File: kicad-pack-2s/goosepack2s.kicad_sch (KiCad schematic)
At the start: 67 parts, among them J1 USB_C_Receptacle_USB2.0_16P, J11 Balance 2S, J2 Pack lead, J3 XT30UPB-M, Q2 IRF8736, Q3 IRF8736, Q4 AO3400A, Q5 AO3400A, U13 HY2120-LB, U21 HY2213-BB3A, U22 HY2213-BB3A, U7 BQ25798

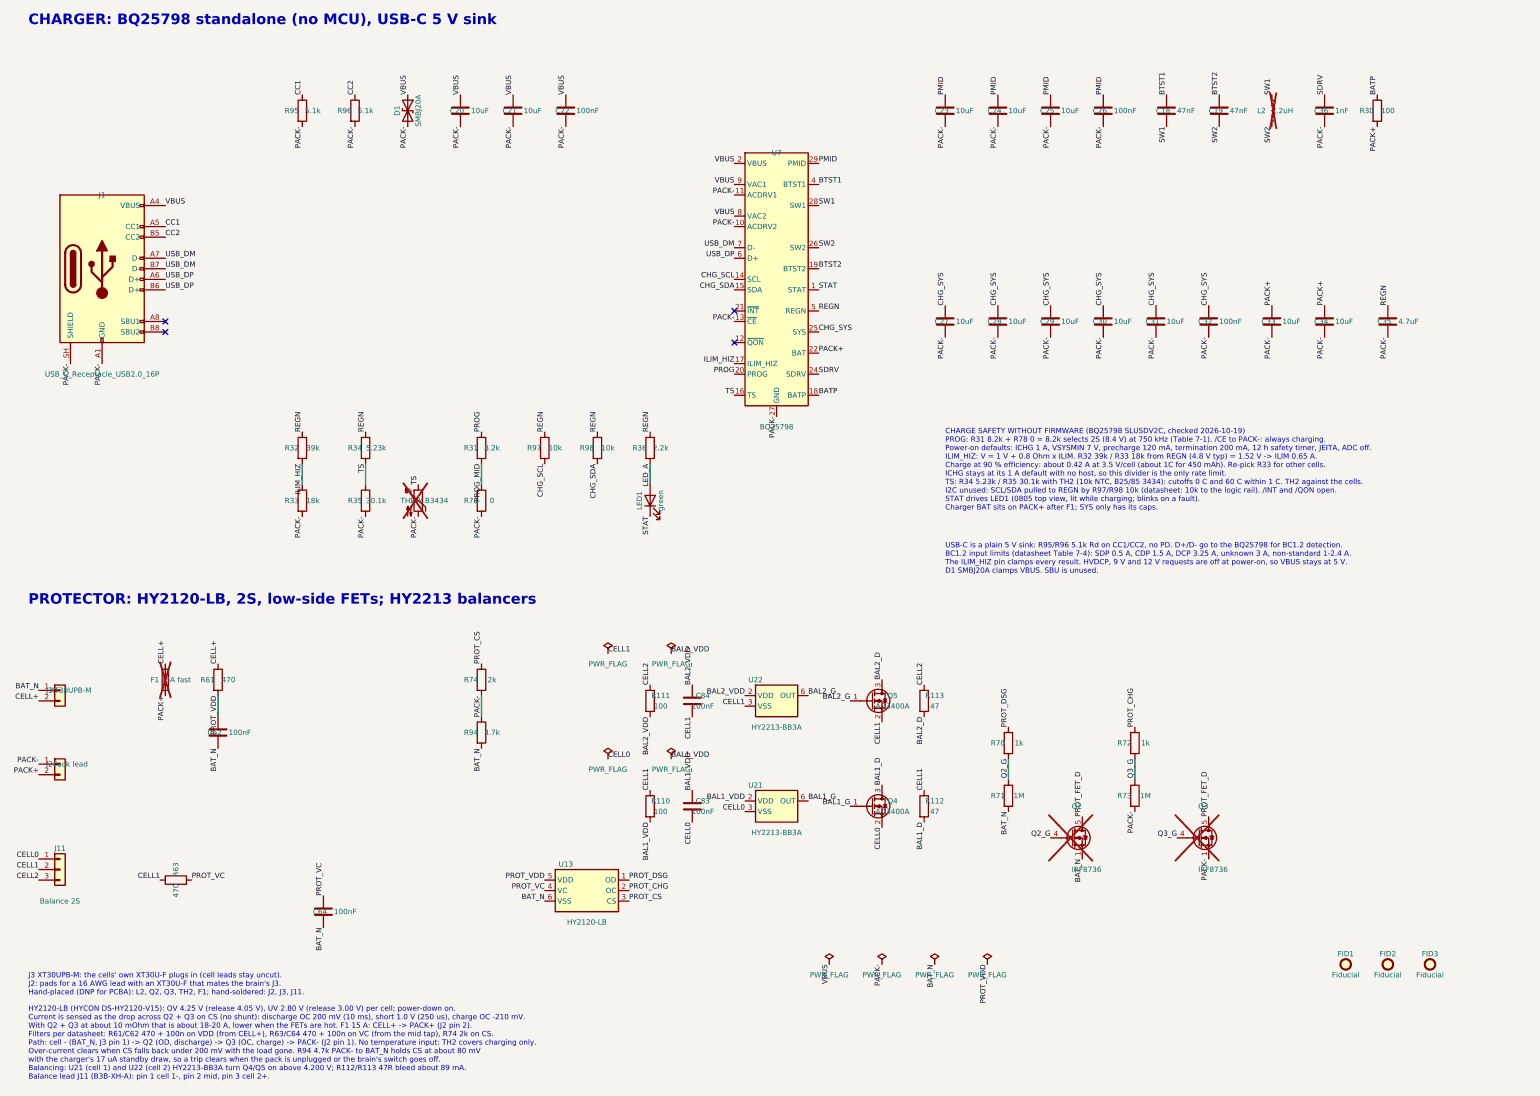
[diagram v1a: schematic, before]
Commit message: Place and route the 2S pack board and add a --board switch to the pack tools
Every pack tool takes --board=pack2s (tools/packcfg.py); the 3S defaults and
placement are unchanged. The 2S board is 45 x 23 mm, routed with grid_router,
DRC-clean with schematic parity. The schematic is synced to the 3S fixes (J2/J3
pigtail pads, 0402 boot caps, SMBJ15A, RALEC R34), JLC places F1, L2, Q2 and Q3,
and TH2 became a fixed 10k R79 as on 3S. docs/2s-pack-process.md lists the
differences from the 3S process.

Co-Authored-By: Claude Opus 5.5 <noreply@anthropic.com>
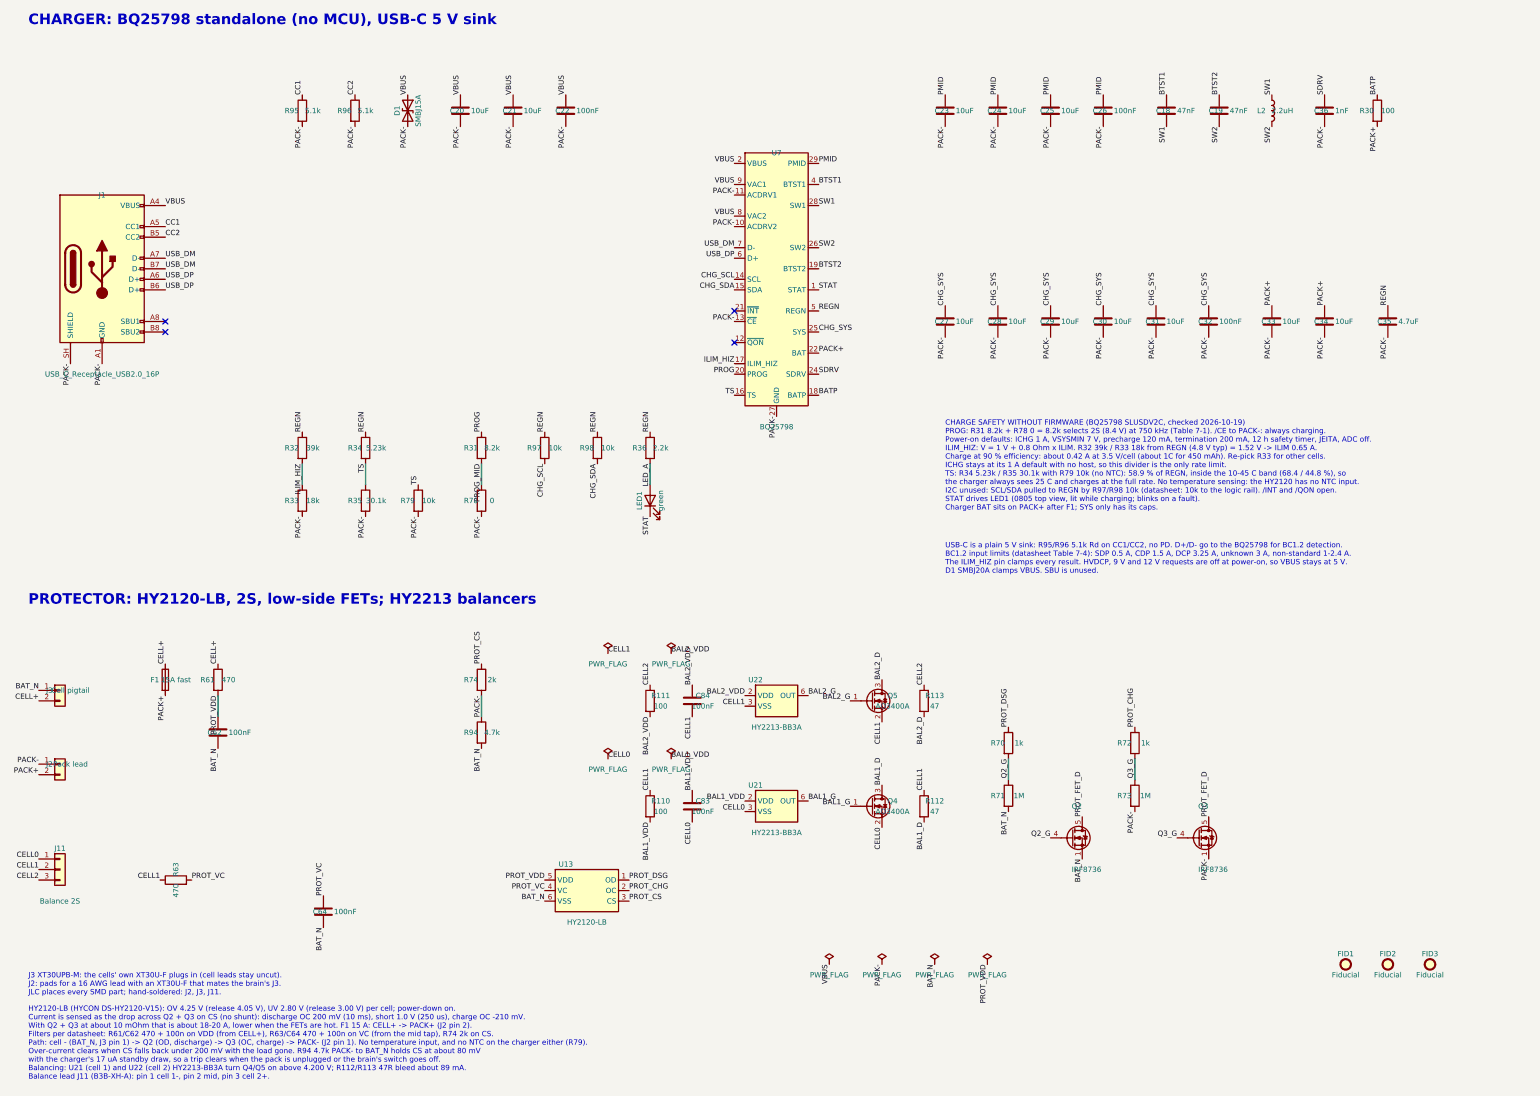
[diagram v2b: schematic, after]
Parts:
- C18, C19: footprint Capacitor_SMD:C_0603_1608Metric -> Capacitor_SMD:C_0402_1005Metric; LCSC Part # C1622 -> C192385; MPN 0603B473K500NT -> 0402B473K160NT
- D1: value SMBJ20A -> SMBJ15A; LCSC Part # C19077575 -> C19077569; MPN SMBJ20A -> SMBJ15A
- F1, L2, Q2, Q3: now fitted
- J2: footprint hexy:XT30_SolderPads_1x02_P5.00mm -> Connector_Wire:SolderWire-1.5sqmm_1x02_P6mm_D1.7mm_OD3mm
- J3: value XT30UPB-M -> Cell pigtail; footprint hexy:AMASS_XT30UPB-M_1x02_P5.0mm_Vertical_EasyEDA3D -> Connector_Wire:SolderWire-1.5sqmm_1x02_P6mm_D1.7mm_OD3mm; LCSC Part # C428721 -> C99101; MPN XT30UPB-M -> XT30U-M
- R34: LCSC Part # C25907 -> C11631; MPN 0402WGF5231TCE -> RTT025231FTH; Manufacturer UNI-ROYAL -> RALEC
- R79: renamed from TH2; value 10k B3434 -> 10k; symbol Device:Thermistor_NTC -> Device:R; LCSC Part # C13564 -> C25804; MPN NCP18XH103F03RB -> 0603WAF1002T5E; Manufacturer Murata -> UNI-ROYAL; now fitted
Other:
- note added: "J3 XT30UPB-M: the cells' own XT30U-F plugs in (cell leads stay uncut). J2: pads for a 16 AWG lead with an XT30U-F that mates the brain's J3. JLC places every SMD part; hand-soldered: J2, J3, J11."
- note removed: "J3 XT30UPB-M: the cells' own XT30U-F plugs in (cell leads stay uncut). J2: pads for a 16 AWG lead with an XT30U-F that mates the brain's J3. Hand-placed (DNP for PCBA): L2, Q2, Q3, TH2, F1; hand-soldered: J2, J3, J11."
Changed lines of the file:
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@@
 			)
 		)
-		(property "Value" "SMBJ20A"
+		(property "Value" "SMBJ15A"
 			(at 116.84 50.8 0)
 			(show_name no)
@@
 			)
 		)
-		(property "MPN" "SMBJ20A"
+		(property "MPN" "SMBJ15A"
 			(at 114.3 50.8 0)
 			(effects
@@
 			)
 		)
-		(property "LCSC Part #" "C19077575"
+		(property "LCSC Part #" "C19077569"
 			(at 114.3 50.8 0)
 			(effects
@@
 			)
 		)
-		(property "MPN" "0402WGF5231TCE"
+		(property "MPN" "RTT025231FTH"
 			(at 104.14 132.08 0)
 			(effects
@@
 			)
 		)
-		(property "Manufacturer" "UNI-ROYAL"
+		(property "Manufacturer" "RALEC"
 			(at 104.14 132.08 0)
 			(effects
@@
 			)
 		)
-		(property "LCSC Part #" "C25907"
+		(property "LCSC Part #" "C11631"
 			(at 104.14 132.08 0)
 			(effects
@@
 	)
 	(symbol
-		(lib_id "Device:Thermistor_NTC")
+		(lib_id "Device:R")
 		(at 116.84 144.78 0)
 		(unit 1)
@@
 		(on_board yes)
 		(in_pos_files yes)
-		(dnp yes)
-		(property "Reference" "TH2"
+		(dnp no)
+		(property "Reference" "R79"
 			(at 114.3 144.78 0)
 			(show_name no)
@@
 			)
 		)
-		(property "Value" "10k B3434"
+		(property "Value" "10k"
 			(at 119.38 144.78 0)
 			(show_name no)
@@
 			)
 		)
-		(property "Description" "Temperature dependent resistor, negative temperature coefficient"
+		(property "Description" "Resistor"
 			(at 116.84 144.78 0)
 			(hide yes)
@@
 			)
 		)
-		(property "MPN" "NCP18XH103F03RB"
+		(property "MPN" "0603WAF1002T5E"
 			(at 116.84 144.78 0)
 			(effects
@@
 			)
 		)
-		(property "Manufacturer" "Murata"
+		(property "Manufacturer" "UNI-ROYAL"
 			(at 116.84 144.78 0)
 			(effects
@@
 			)
 		)
-		(property "LCSC Part #" "C13564"
+		(property "LCSC Part #" "C25804"
 			(at 116.84 144.78 0)
 			(effects
@@
 			(project "goosepack2s"
 				(path "/b039c4cd-30f0-48b1-bce5-22fee9821a58"
-					(reference "TH2")
+					(reference "R79")
 					(unit 1)
 				)
@@
 			)
 		)
-		(property "Footprint" "Capacitor_SMD:C_0603_1608Metric"
+		(property "Footprint" "Capacitor_SMD:C_0402_1005Metric"
 			(at 298.145 46.99 0)
 			(hide yes)
@@
 			)
 		)
-		(property "MPN" "0603B473K500NT"
+		(property "MPN" "0402B473K160NT"
 			(at 297.18 50.8 0)
 			(effects
@@
 			)
 		)
-		(property "LCSC Part #" "C1622"
+		(property "LCSC Part #" "C192385"
 			(at 297.18 50.8 0)
 			(effects
@@
 			)
 		)
-		(property "Footprint" "Capacitor_SMD:C_0603_1608Metric"
+		(property "Footprint" "Capacitor_SMD:C_0402_1005Metric"
 			(at 310.845 46.99 0)
 			(hide yes)
@@
 			)
 		)
-		(property "MPN" "0603B473K500NT"
+		(property "MPN" "0402B473K160NT"
 			(at 309.88 50.8 0)
 			(effects
@@
 			)
 		)
-		(property "LCSC Part #" "C1622"
+		(property "LCSC Part #" "C192385"
 			(at 309.88 50.8 0)
 			(effects
@@
 		(on_board yes)
 		(in_pos_files yes)
-		(dnp yes)
+		(dnp no)
 		(property "Reference" "L2"
 			(at 320.04 50.8 0)
@@
 			)
 		)
-		(property "Value" "XT30UPB-M"
+		(property "Value" "Cell pigtail"
 			(at 33.02 190.5 0)
 			(show_name no)
@@
 			)
 		)
-		(property "Footprint" "hexy:AMASS_XT30UPB-M_1x02_P5.0mm_Vertical_EasyEDA3D"
+		(property "Footprint" "Connector_Wire:SolderWire-1.5sqmm_1x02_P6mm_D1.7mm_OD3mm"
 			(at 30.48 190.5 0)
 			(hide yes)
@@
 			)
 		)
-		(property "MPN" "XT30UPB-M"
+		(property "MPN" "XT30U-M"
 			(at 30.48 190.5 0)
 			(effects
@@
 			)
 		)
-		(property "LCSC Part #" "C428721"
+		(property "LCSC Part #" "C99101"
 			(at 30.48 190.5 0)
 			(effects
@@
 			)
 		)
-		(property "Footprint" "hexy:XT30_SolderPads_1x02_P5.00mm"
+		(property "Footprint" "Connector_Wire:SolderWire-1.5sqmm_1x02_P6mm_D1.7mm_OD3mm"
 			(at 30.48 208.28 0)
 			(hide yes)
@@
 		(on_board yes)
 		(in_pos_files yes)
-		(dnp yes)
+		(dnp no)
 		(property "Reference" "F1"
 			(at 53.34 187.96 0)
@@
 		(on_board yes)
 		(in_pos_files yes)
-		(dnp yes)
+		(dnp no)
 		(property "Reference" "Q2"
 			(at 274.32 218.44 0)
@@
 		(on_board yes)
 		(in_pos_files yes)
-		(dnp yes)
+		(dnp no)
 		(property "Reference" "Q3"
 			(at 304.8 218.44 0)
@@
 		)
 	)
-	(text "CHARGE SAFETY WITHOUT FIRMWARE (BQ25798 SLUSDV2C, checked 2026-10-19)\nPROG: R31 8.2k + R78 0 = 8.2k selects 2S (8.4 V) at 750 kHz (Table 7-1). /CE to PACK-: always charging.\nPower-on defaults: ICHG 1 A, VSYSMIN 7 V, precharge 120 mA, termination 200 mA, 12 h safety timer, JEITA, ADC off.\nILIM_HIZ: V = 1 V + 0.8 Ohm x ILIM. R32 39k / R33 18k from REGN (4.8 V typ) = 1.52 V -> ILIM 0.65 A.\nCharge at 90 % efficiency: about 0.42 A at 3.5 V/cell (about 1C for 450 mAh). Re-pick R33 for other cells.\nICHG stays at its 1 A default with no host, so this divider is the only rate limit.\nTS: R34 5.23k / R35 30.1k with TH2 (10k NTC, B25/85 3434): cutoffs 0 C and 60 C within 1 C. TH2 against the cells.\nI2C unused: SCL/SDA pulled to REGN by R97/R98 10k (datasheet: 10k to the logic rail). /INT and /QON open.\nSTAT drives LED1 (0805 top view, lit while charging; blinks on a fault).\nCharger BAT sits on PACK+ after F1; SYS only has its caps."
+	(text "CHARGE SAFETY WITHOUT FIRMWARE (BQ25798 SLUSDV2C, checked 2026-10-19)\nPROG: R31 8.2k + R78 0 = 8.2k selects 2S (8.4 V) at 750 kHz (Table 7-1). /CE to PACK-: always charging.\nPower-on defaults: ICHG 1 A, VSYSMIN 7 V, precharge 120 mA, termination 200 mA, 12 h safety timer, JEITA, ADC off.\nILIM_HIZ: V = 1 V + 0.8 Ohm x ILIM. R32 39k / R33 18k from REGN (4.8 V typ) = 1.52 V -> ILIM 0.65 A.\nCharge at 90 % efficiency: about 0.42 A at 3.5 V/cell (about 1C for 450 mAh). Re-pick R33 for other cells.\nICHG stays at its 1 A default with no host, so this divider is the only rate limit.\nTS: R34 5.23k / R35 30.1k with R79 10k (no NTC): 58.9 % of REGN, inside the 10-45 C band (68.4 / 44.8 %), so\nthe charger always sees 25 C and charges at the full rate. No temperature sensing: the HY2120 has no NTC input.\nI2C unused: SCL/SDA pulled to REGN by R97/R98 10k (datasheet: 10k to the logic rail). /INT and /QON open.\nSTAT drives LED1 (0805 top view, lit while charging; blinks on a fault).\nCharger BAT sits on PACK+ after F1; SYS only has its caps."
 		(exclude_from_sim no)
 		(at 243.84 147.32 0)
@@
 		)
 	)
-	(text "HY2120-LB (HYCON DS-HY2120-V15): OV 4.25 V (release 4.05 V), UV 2.80 V (release 3.00 V) per cell; power-down on.\nCurrent is sensed as the drop across Q2 + Q3 on CS (no shunt): discharge OC 200 mV (10 ms), short 1.0 V (250 us), charge OC -210 mV.\nWith Q2 + Q3 at about 10 mOhm that is about 18-20 A, lower when the FETs are hot. F1 15 A: CELL+ -> PACK+ (J2 pin 2).\nFilters per datasheet: R61/C62 470 + 100n on VDD (from CELL+), R63/C64 470 + 100n on VC (from the mid tap), R74 2k on CS.\nPath: cell - (BAT_N, J3 pin 1) -> Q2 (OD, discharge) -> Q3 (OC, charge) -> PACK- (J2 pin 1). No temperature input: TH2 covers charging only.\nOver-current clears when CS falls back under 200 mV with the load gone. R94 4.7k PACK- to BAT_N holds CS at about 80 mV\nwith the charger's 17 uA standby draw, so a trip clears when the pack is unplugged or the brain's switch goes off.\nBalancing: U21 (cell 1) and U22 (cell 2) HY2213-BB3A turn Q4/Q5 on above 4.200 V; R112/R113 47R bleed about 89 mA.\nBalance lead J11 (B3B-XH-A): pin 1 cell 1-, pin 2 mid, pin 3 cell 2+."
+	(text "HY2120-LB (HYCON DS-HY2120-V15): OV 4.25 V (release 4.05 V), UV 2.80 V (release 3.00 V) per cell; power-down on.\nCurrent is sensed as the drop across Q2 + Q3 on CS (no shunt): discharge OC 200 mV (10 ms), short 1.0 V (250 us), charge OC -210 mV.\nWith Q2 + Q3 at about 10 mOhm that is about 18-20 A, lower when the FETs are hot. F1 15 A: CELL+ -> PACK+ (J2 pin 2).\nFilters per datasheet: R61/C62 470 + 100n on VDD (from CELL+), R63/C64 470 + 100n on VC (from the mid tap), R74 2k on CS.\nPath: cell - (BAT_N, J3 pin 1) -> Q2 (OD, discharge) -> Q3 (OC, charge) -> PACK- (J2 pin 1). No temperature input, and no NTC on the charger either (R79).\nOver-current clears when CS falls back under 200 mV with the load gone. R94 4.7k PACK- to BAT_N holds CS at about 80 mV\nwith the charger's 17 uA standby draw, so a trip clears when the pack is unplugged or the brain's switch goes off.\nBalancing: U21 (cell 1) and U22 (cell 2) HY2213-BB3A turn Q4/Q5 on above 4.200 V; R112/R113 47R bleed about 89 mA.\nBalance lead J11 (B3B-XH-A): pin 1 cell 1-, pin 2 mid, pin 3 cell 2+."
 		(exclude_from_sim no)
 		(at 22.86 284.48 0)
@@
 		)
 	)
-	(text "J3 XT30UPB-M: the cells' own XT30U-F plugs in (cell leads stay uncut).\nJ2: pads for a 16 AWG lead with an XT30U-F that mates the brain's J3.\nHand-placed (DNP for PCBA): L2, Q2, Q3, TH2, F1; hand-soldered: J2, J3, J11."
+	(text "J3 XT30UPB-M: the cells' own XT30U-F plugs in (cell leads stay uncut).\nJ2: pads for a 16 AWG lead with an XT30U-F that mates the brain's J3.\nJLC places every SMD part; hand-soldered: J2, J3, J11."
 		(exclude_from_sim no)
 		(at 22.86 264.16 0)
